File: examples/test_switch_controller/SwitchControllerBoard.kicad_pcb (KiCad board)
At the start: 2 copper layers, 64 x 35 mm, 40 parts, among them J1 COM-15111 (Sparkfun), J2 PinHeader2.54 1x4 (Generic), J3 PinHeader2.54 1x4 (Generic), Q1 2N7002 (Changjiang Electronic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, Q2 AO3401A (Alpha & Omega Semico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, SW1 5.1mm switch, SW2 5.1mm switch, U1 LD1117S33TR (STMicroelectroni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, U2 ESP32-WROOM-32 (Espressif Sys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, U3 LMV321 (Texas Instruments), U4 Duck, U5 IdDots4

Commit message: wip
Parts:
- added C10: , Capacitor_SMD:C_0805_2012Metric, F.Cu at (175.8, 40.2)
- added C11: , Capacitor_SMD:C_0603_1608Metric, F.Cu at (184.4, 37.0)
- added C12: , Capacitor_SMD:C_0805_2012Metric, F.Cu at (175.8, 37.2)
- added C13: , Capacitor_SMD:C_0603_1608Metric, F.Cu at (204.1, 26.2)
- added C14: , Capacitor_SMD:C_0603_1608Metric, F.Cu at (204.1, 28.7)
- added C15: , Capacitor_SMD:C_0603_1608Metric, F.Cu at (204.1, 23.7)
- added C6: , Capacitor_SMD:C_0603_1608Metric, F.Cu at (175.5, 43.0)
- added C7: , Capacitor_SMD:C_0603_1608Metric, F.Cu at (180.0, 40.0)
- added C8: , Capacitor_SMD:C_0805_2012Metric, F.Cu at (180.2, 37.2)
- added C9: , Capacitor_SMD:C_0603_1608Metric, F.Cu at (179.6, 43.0)
- added J3: AFC01-S015FCA-00 (Jushuo), Connector_FFC-FPC:Hirose_FH12-15S-0.5SH_1x15-1MP_P0.50mm_Horizontal, F.Cu at (180.9, 26.0)
- added R7: , Resistor_SMD:R_0603_1608Metric, F.Cu at (184.0, 40.0)
- added U3: CP2102 (Silicon Labs), Package_DFN_QFN:QFN-28-1EP_5x5mm_P0.5mm_EP3.35x3.35mm, F.Cu at (198.5, 26.1)
- added U4: PESD5V0X1BT (Nexperia), Package_TO_SOT_SMD:SOT-23, F.Cu at (194.2, 38.0)
- renumbered C6 to C16, J3 to J4, R9 to R10, R10 to R11, R11 to R12, R12 to R13, R7 to R8, R8 to R9, U3 to U5, U4 to U6, U5 to U7
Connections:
- U2 pad 10: sw1.out -> lcd.spi.miso
- U2 pad 11: ledr.signal -> usb_uart.uart.rx
- U2 pad 12: ledg.signal -> usb_uart.uart.tx
- U2 pad 13: ledb.signal -> conn.uart.rx
- U2 pad 14: sw.control -> conn.uart.tx
- U2 pad 16: (no net) -> sw1.out
- U2 pad 23: (no net) -> ledr.signal
- U2 pad 26: (no net) -> ledg.signal
- U2 pad 27: (no net) -> ledb.signal
- U2 pad 28: (no net) -> lcd.cs
- U2 pad 29: (no net) -> lcd.reset
- U2 pad 30: (no net) -> lcd.dc
- U2 pad 37: (no net) -> sw.control
- U2 pad 8: conn.uart.rx -> lcd.spi.sck
- U2 pad 9: conn.uart.tx -> lcd.spi.mosi

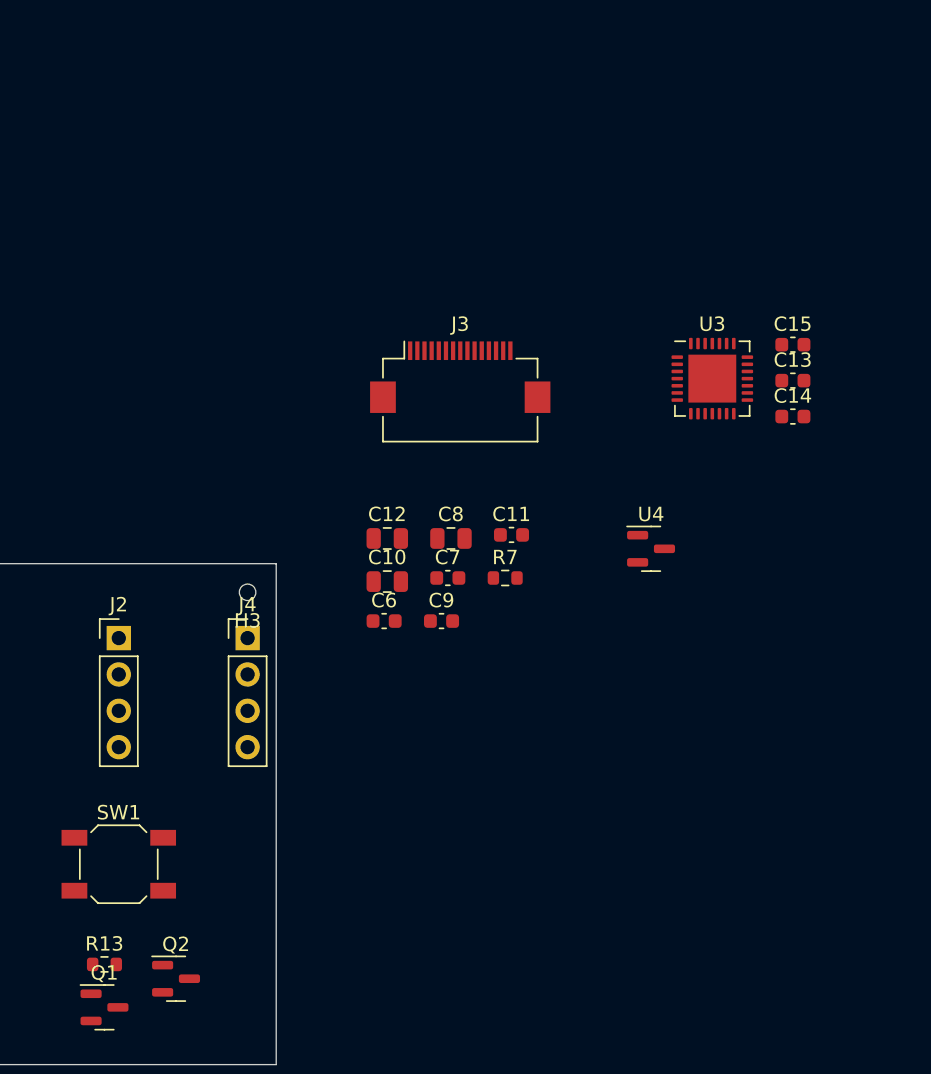
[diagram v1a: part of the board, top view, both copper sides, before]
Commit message: OLED outline
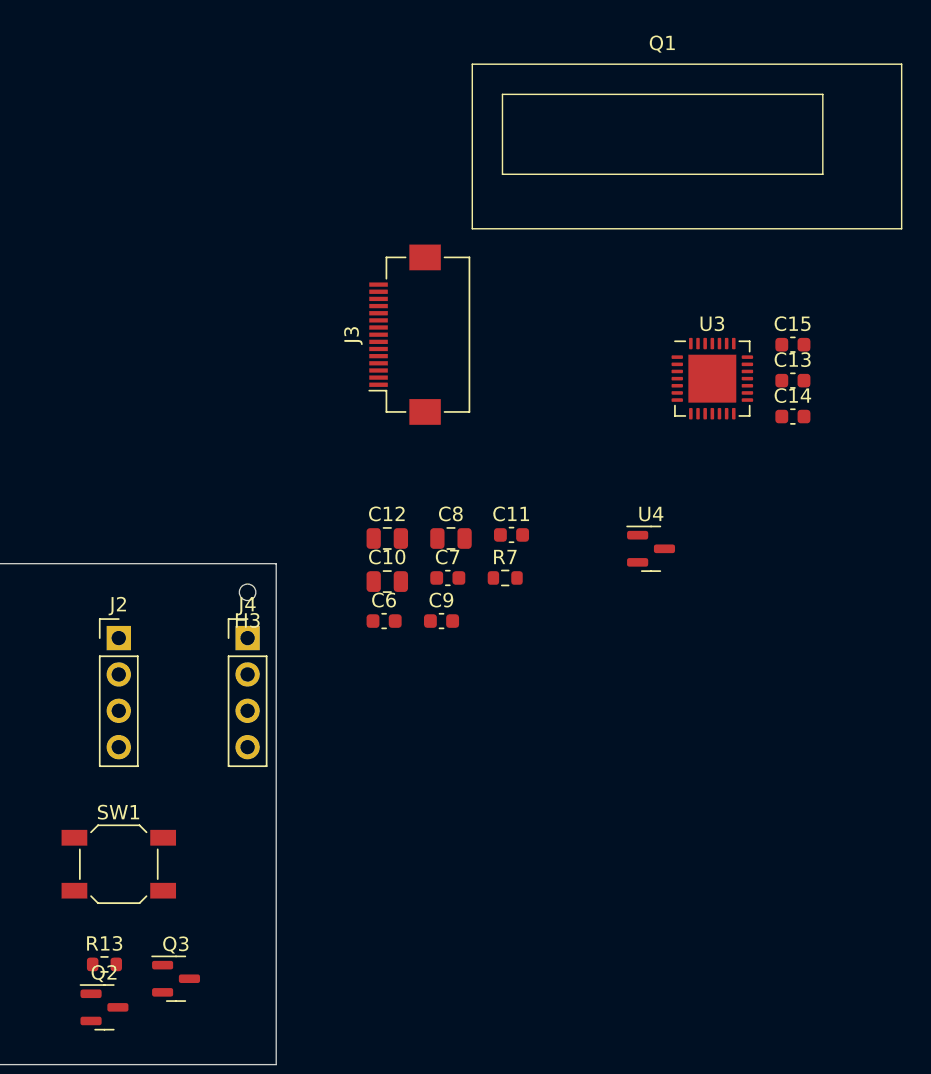
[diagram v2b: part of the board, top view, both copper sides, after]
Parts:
- added Q1: ER-OLED-0.91-e (EastRising), edg:Lcd_Er_Oled0.91_3_Outline, F.Cu at (195.0, 9.00)
- moved J3 4.87 mm to (177.0, 23.0), turned to 90 degrees
- renumbered Q1 to Q2, Q2 to Q3
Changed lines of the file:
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@@
   )
   (footprint "Connector_FFC-FPC:Hirose_FH12-15S-0.5SH_1x15-1MP_P0.50mm_Horizontal" (layer "F.Cu")
-    (at 180.86 25.97)
+    (at 177 23 90)
     (descr "Hirose FH12, FFC/FPC connector, FH12-15S-0.5SH, 15 Pins per row (https://www.hirose.com/product/en/products/FH12/FH12-24S-0.5SH(55)/), generated with kicad-footprint-generator")
     (tags "connector Hirose FH12 horizontal")
@@
     (property "edg_short_path" "lcd.device.conn")
     (attr smd)
-    (fp_text reference "J3" (at 0 -3.7) (layer "F.SilkS")
-      (effects (font (size 1 1) (thickness 0.15)))
-    )
-    (fp_text value "AFC01-S015FCA-00 (Jushuo)" (at 0 5.6) (layer "F.Fab")
-      (effects (font (size 1 1) (thickness 0.15)))
-    )
-    (fp_text user "${REFERENCE}" (at 0 3.7) (layer "F.Fab")
+    (fp_text reference "J3" (at 0 -3.7 90) (layer "F.SilkS")
+      (effects (font (size 1 1) (thickness 0.15)))
+    )
+    (fp_text value "AFC01-S015FCA-00 (Jushuo)" (at 0 5.6 90) (layer "F.Fab")
+      (effects (font (size 1 1) (thickness 0.15)))
+    )
+    (fp_text user "${REFERENCE}" (at 0 3.7 90) (layer "F.Fab")
       (effects (font (size 1 1) (thickness 0.15)))
     )
@@
     (fp_line (start 5.2 4.4) (end 0 4.4) (layer "F.Fab") (width 0.1))
     (fp_line (start -4.7 3.4) (end -4.7 3.7) (layer "F.Fab") (width 0.1))
-    (pad "1" smd rect (at -3.5 -1.85) (size 0.3 1.3) (layers "F.Cu" "F.Paste" "F.Mask")
+    (pad "1" smd rect (at -3.5 -1.85 90) (size 0.3 1.3) (layers "F.Cu" "F.Paste" "F.Mask")
       (net 47 "lcd.c2_cap.pos"))
-    (pad "2" smd rect (at -3 -1.85) (size 0.3 1.3) (layers "F.Cu" "F.Paste" "F.Mask")
+    (pad "2" smd rect (at -3 -1.85 90) (size 0.3 1.3) (layers "F.Cu" "F.Paste" "F.Mask")
       (net 48 "lcd.c2_cap.neg"))
-    (pad "3" smd rect (at -2.5 -1.85) (size 0.3 1.3) (layers "F.Cu" "F.Paste" "F.Mask")
+    (pad "3" smd rect (at -2.5 -1.85 90) (size 0.3 1.3) (layers "F.Cu" "F.Paste" "F.Mask")
       (net 49 "lcd.c1_cap.pos"))
-    (pad "4" smd rect (at -2 -1.85) (size 0.3 1.3) (layers "F.Cu" "F.Paste" "F.Mask")
+    (pad "4" smd rect (at -2 -1.85 90) (size 0.3 1.3) (layers "F.Cu" "F.Paste" "F.Mask")
       (net 50 "lcd.c1_cap.neg"))
-    (pad "5" smd rect (at -1.5 -1.85) (size 0.3 1.3) (layers "F.Cu" "F.Paste" "F.Mask")
+    (pad "5" smd rect (at -1.5 -1.85 90) (size 0.3 1.3) (layers "F.Cu" "F.Paste" "F.Mask")
       (net 17 "v3v3"))
-    (pad "6" smd rect (at -1 -1.85) (size 0.3 1.3) (layers "F.Cu" "F.Paste" "F.Mask")
-      (net 1 "gnd"))
-    (pad "7" smd rect (at -0.5 -1.85) (size 0.3 1.3) (layers "F.Cu" "F.Paste" "F.Mask")
+    (pad "6" smd rect (at -1 -1.85 90) (size 0.3 1.3) (layers "F.Cu" "F.Paste" "F.Mask")
+      (net 1 "gnd"))
+    (pad "7" smd rect (at -0.5 -1.85 90) (size 0.3 1.3) (layers "F.Cu" "F.Paste" "F.Mask")
       (net 17 "v3v3"))
-    (pad "8" smd rect (at 0 -1.85) (size 0.3 1.3) (layers "F.Cu" "F.Paste" "F.Mask")
+    (pad "8" smd rect (at 0 -1.85 90) (size 0.3 1.3) (layers "F.Cu" "F.Paste" "F.Mask")
       (net 35 "lcd.cs"))
-    (pad "9" smd rect (at 0.5 -1.85) (size 0.3 1.3) (layers "F.Cu" "F.Paste" "F.Mask")
+    (pad "9" smd rect (at 0.5 -1.85 90) (size 0.3 1.3) (layers "F.Cu" "F.Paste" "F.Mask")
       (net 36 "lcd.reset"))
-    (pad "10" smd rect (at 1 -1.85) (size 0.3 1.3) (layers "F.Cu" "F.Paste" "F.Mask")
+    (pad "10" smd rect (at 1 -1.85 90) (size 0.3 1.3) (layers "F.Cu" "F.Paste" "F.Mask")
       (net 37 "lcd.dc"))
-    (pad "11" smd rect (at 1.5 -1.85) (size 0.3 1.3) (layers "F.Cu" "F.Paste" "F.Mask")
+    (pad "11" smd rect (at 1.5 -1.85 90) (size 0.3 1.3) (layers "F.Cu" "F.Paste" "F.Mask")
       (net 30 "lcd.spi.sck"))
-    (pad "12" smd rect (at 2 -1.85) (size 0.3 1.3) (layers "F.Cu" "F.Paste" "F.Mask")
+    (pad "12" smd rect (at 2 -1.85 90) (size 0.3 1.3) (layers "F.Cu" "F.Paste" "F.Mask")
       (net 31 "lcd.spi.mosi"))
-    (pad "13" smd rect (at 2.5 -1.85) (size 0.3 1.3) (layers "F.Cu" "F.Paste" "F.Mask")
+    (pad "13" smd rect (at 2.5 -1.85 90) (size 0.3 1.3) (layers "F.Cu" "F.Paste" "F.Mask")
       (net 29 "lcd.iref_res.a"))
-    (pad "14" smd rect (at 3 -1.85) (size 0.3 1.3) (layers "F.Cu" "F.Paste" "F.Mask")
+    (pad "14" smd rect (at 3 -1.85 90) (size 0.3 1.3) (layers "F.Cu" "F.Paste" "F.Mask")
       (net 51 "lcd.device.vcomh"))
-    (pad "15" smd rect (at 3.5 -1.85) (size 0.3 1.3) (layers "F.Cu" "F.Paste" "F.Mask")
+    (pad "15" smd rect (at 3.5 -1.85 90) (size 0.3 1.3) (layers "F.Cu" "F.Paste" "F.Mask")
       (net 52 "lcd.device.vcc"))
-    (pad "MP" smd rect (at 5.4 1.4) (size 1.8 2.2) (layers "F.Cu" "F.Paste" "F.Mask"))
-    (pad "MP" smd rect (at -5.4 1.4) (size 1.8 2.2) (layers "F.Cu" "F.Paste" "F.Mask"))
+    (pad "MP" smd rect (at 5.4 1.4 90) (size 1.8 2.2) (layers "F.Cu" "F.Paste" "F.Mask"))
+    (pad "MP" smd rect (at -5.4 1.4 90) (size 1.8 2.2) (layers "F.Cu" "F.Paste" "F.Mask"))
     (model "${KICAD6_3DMODEL_DIR}/Connector_FFC-FPC.3dshapes/Hirose_FH12-15S-0.5SH_1x15-1MP_P0.50mm_Horizontal.wrl"
       (offset (xyz 0 0 0))
@@
     (property "edg_part" "2N7002 (Changjiang Electronics Tech (CJ))")
     (property "edg_path" "sw.pre")
-    (property "edg_refdes" "Q1")
+    (property "edg_refdes" "Q2")
     (property "edg_short_path" "sw.pre")
     (attr smd)
-    (fp_text reference "Q1" (at 0 -2.4) (layer "F.SilkS")
+    (fp_text reference "Q2" (at 0 -2.4) (layer "F.SilkS")
       (effects (font (size 1 1) (thickness 0.15)))
     )
@@
     (property "edg_part" "AO3401A (Alpha & Omega Semicon)")
     (property "edg_path" "sw.drv")
-    (property "edg_refdes" "Q2")
+    (property "edg_refdes" "Q3")
     (property "edg_short_path" "sw.drv")
     (attr smd)
-    (fp_text reference "Q2" (at 0 -2.4) (layer "F.SilkS")
+    (fp_text reference "Q3" (at 0 -2.4) (layer "F.SilkS")
       (effects (font (size 1 1) (thickness 0.15)))
     )
@@
     )
   )
+  (footprint "edg:Lcd_Er_Oled0.91_3_Outline" (layer "F.Cu")
+    (at 195 9)
+    (descr "Outline for the ER-OLED0.91-3 series OLEDs. Connector placement (on User.Comments layer, with FPC folded over underneath the board, for a bottom-entry FPC connector) is from the Reference Mechanical Design.")
+    (property "Sheetfile" "electronics_lib.Oled_Er_Oled_091_3.Er_Oled_091_3_Device")
+    (property "Sheetname" "device")
+    (property "edg_part" "ER-OLED-0.91-e (EastRising)")
+    (property "edg_path" "lcd.device.lcd")
+    (property "edg_refdes" "Q1")
+    (property "edg_short_path" "lcd.device.lcd")
+    (attr exclude_from_pos_files)
+    (fp_text reference "Q1" (at 0 -6.35) (layer "F.SilkS")
+      (effects (font (size 1 1) (thickness 0.15)))
+    )
+    (fp_text value "ER-OLED-0.91-e (EastRising)" (at 0 7.62) (layer "F.Fab")
+      (effects (font (size 1 1) (thickness 0.15)))
+    )
+    (fp_line (start -13.3 -4.9) (end -13.3 6.6) (layer "F.SilkS") (width 0.1))
+    (fp_line (start -11.192 -2.792) (end 11.192 -2.792) (layer "F.SilkS") (width 0.1))
+    (fp_line (start -13.3 6.6) (end 16.7 6.6) (layer "F.SilkS") (width 0.1))
+    (fp_line (start 16.7 -4.9) (end -13.3 -4.9) (layer "F.SilkS") (width 0.1))
+    (fp_line (start 11.192 -2.792) (end 11.192 2.792) (layer "F.SilkS") (width 0.1))
+    (fp_line (start 11.192 2.792) (end -11.192 2.792) (layer "F.SilkS") (width 0.1))
+    (fp_line (start -11.192 2.792) (end -11.192 -2.792) (layer "F.SilkS") (width 0.1))
+    (fp_line (start 16.7 6.6) (end 16.7 -4.9) (layer "F.SilkS") (width 0.1))
+    (fp_line (start 10.71 -2.04) (end 8.21 -2.04) (layer "Cmts.User") (width 0.12))
+    (fp_line (start 8.21 5.96) (end 10.71 5.96) (layer "Cmts.User") (width 0.12))
+    (fp_line (start 8.71 4.96) (end 8.71 4.96) (layer "Cmts.User") (width 0.25))
+    (fp_line (start 18.3 5.96) (end 18.3 -2.04) (layer "Cmts.User") (width 0.12))
+    (fp_line (start 8.21 5.96) (end 8.21 -2.04) (layer "Cmts.User") (width 0.12))
+  )
   (gr_rect (start 104 39) (end 168 74) (layer "Edge.Cuts") (width 0.0381) (fill none))

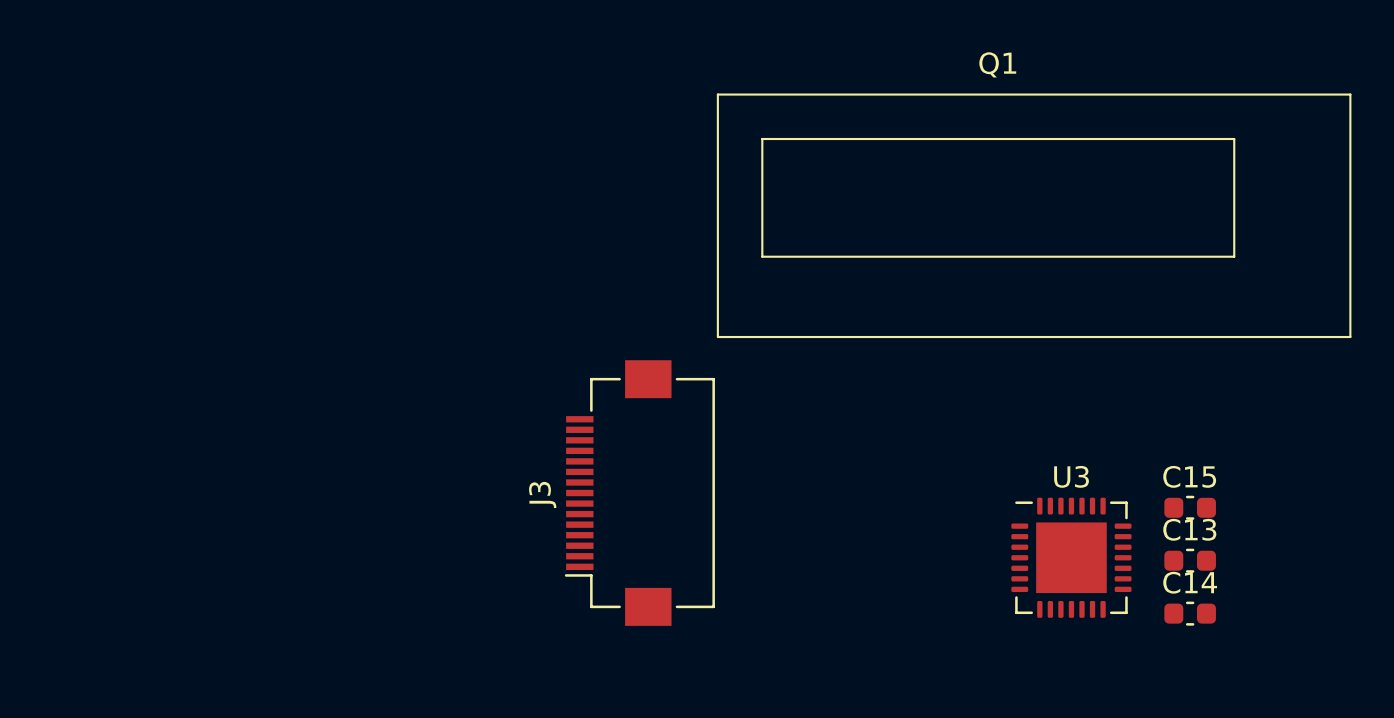
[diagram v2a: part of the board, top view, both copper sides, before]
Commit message: fix footprint
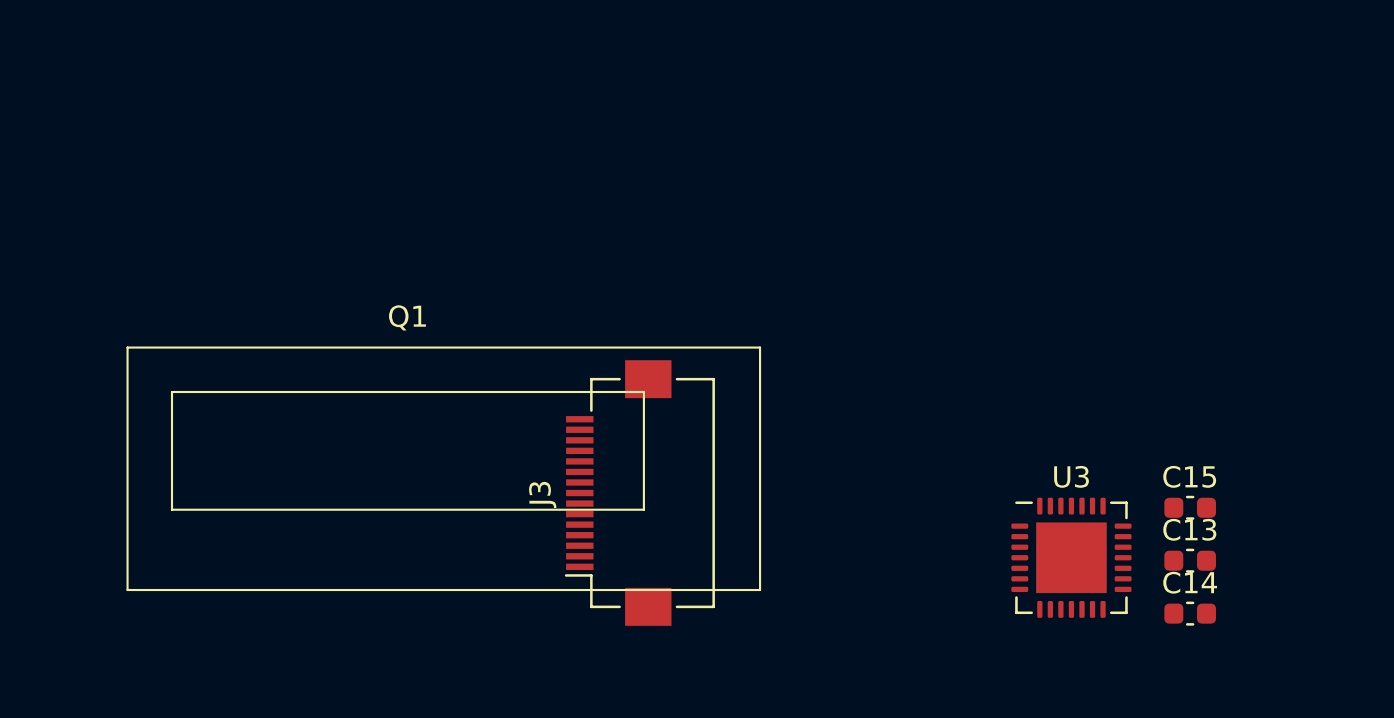
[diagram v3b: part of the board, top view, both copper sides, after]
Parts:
- moved Q1 30.5 mm to (167.0, 21.0)
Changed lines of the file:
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@@
     )
+  )
+  (footprint "edg:Lcd_Er_Oled0.91_3_Outline" (layer "F.Cu")
+    (at 167 21)
+    (descr "Outline for the ER-OLED0.91-3 series OLEDs. Connector placement (on User.Comments layer, with FPC folded over underneath the board, for a bottom-entry FPC connector) is from the Reference Mechanical Design.")
+    (property "Sheetfile" "electronics_lib.Oled_Er_Oled_091_3.Er_Oled_091_3_Device")
+    (property "Sheetname" "device")
+    (property "edg_part" "ER-OLED-0.91-e (EastRising)")
+    (property "edg_path" "lcd.device.lcd")
+    (property "edg_refdes" "Q1")
+    (property "edg_short_path" "lcd.device.lcd")
+    (attr exclude_from_pos_files)
+    (fp_text reference "Q1" (at 0 -6.35) (layer "F.SilkS")
+      (effects (font (size 1 1) (thickness 0.15)))
+    )
+    (fp_text value "ER-OLED-0.91-e (EastRising)" (at 0 7.62) (layer "F.Fab")
+      (effects (font (size 1 1) (thickness 0.15)))
+    )
+    (fp_line (start -13.3 6.6) (end 16.7 6.6) (layer "F.SilkS") (width 0.1))
+    (fp_line (start 11.192 2.792) (end -11.192 2.792) (layer "F.SilkS") (width 0.1))
+    (fp_line (start -13.3 -4.9) (end -13.3 6.6) (layer "F.SilkS") (width 0.1))
+    (fp_line (start 11.192 -2.792) (end 11.192 2.792) (layer "F.SilkS") (width 0.1))
+    (fp_line (start 16.7 6.6) (end 16.7 -4.9) (layer "F.SilkS") (width 0.1))
+    (fp_line (start -11.192 2.792) (end -11.192 -2.792) (layer "F.SilkS") (width 0.1))
+    (fp_line (start -11.192 -2.792) (end 11.192 -2.792) (layer "F.SilkS") (width 0.1))
+    (fp_line (start 16.7 -4.9) (end -13.3 -4.9) (layer "F.SilkS") (width 0.1))
+    (fp_line (start 10.71 -2.04) (end 8.21 -2.04) (layer "Cmts.User") (width 0.12))
+    (fp_line (start 8.21 5.96) (end 8.21 -2.04) (layer "Cmts.User") (width 0.12))
+    (fp_line (start 8.71 5.46) (end 8.71 5.46) (layer "Cmts.User") (width 0.25))
+    (fp_line (start 8.21 5.96) (end 10.71 5.96) (layer "Cmts.User") (width 0.12))
+    (fp_line (start 18.3 5.96) (end 18.3 -2.04) (layer "Cmts.User") (width 0.12))
   )
   (footprint "Package_TO_SOT_SMD:SOT-223-3_TabPin2" (layer "F.Cu")
@@
     )
   )
-  (footprint "edg:Lcd_Er_Oled0.91_3_Outline" (layer "F.Cu")
-    (at 195 9)
-    (descr "Outline for the ER-OLED0.91-3 series OLEDs. Connector placement (on User.Comments layer, with FPC folded over underneath the board, for a bottom-entry FPC connector) is from the Reference Mechanical Design.")
-    (property "Sheetfile" "electronics_lib.Oled_Er_Oled_091_3.Er_Oled_091_3_Device")
-    (property "Sheetname" "device")
-    (property "edg_part" "ER-OLED-0.91-e (EastRising)")
-    (property "edg_path" "lcd.device.lcd")
-    (property "edg_refdes" "Q1")
-    (property "edg_short_path" "lcd.device.lcd")
-    (attr exclude_from_pos_files)
-    (fp_text reference "Q1" (at 0 -6.35) (layer "F.SilkS")
-      (effects (font (size 1 1) (thickness 0.15)))
-    )
-    (fp_text value "ER-OLED-0.91-e (EastRising)" (at 0 7.62) (layer "F.Fab")
-      (effects (font (size 1 1) (thickness 0.15)))
-    )
-    (fp_line (start -13.3 -4.9) (end -13.3 6.6) (layer "F.SilkS") (width 0.1))
-    (fp_line (start -11.192 -2.792) (end 11.192 -2.792) (layer "F.SilkS") (width 0.1))
-    (fp_line (start -13.3 6.6) (end 16.7 6.6) (layer "F.SilkS") (width 0.1))
-    (fp_line (start 16.7 -4.9) (end -13.3 -4.9) (layer "F.SilkS") (width 0.1))
-    (fp_line (start 11.192 -2.792) (end 11.192 2.792) (layer "F.SilkS") (width 0.1))
-    (fp_line (start 11.192 2.792) (end -11.192 2.792) (layer "F.SilkS") (width 0.1))
-    (fp_line (start -11.192 2.792) (end -11.192 -2.792) (layer "F.SilkS") (width 0.1))
-    (fp_line (start 16.7 6.6) (end 16.7 -4.9) (layer "F.SilkS") (width 0.1))
-    (fp_line (start 10.71 -2.04) (end 8.21 -2.04) (layer "Cmts.User") (width 0.12))
-    (fp_line (start 8.21 5.96) (end 10.71 5.96) (layer "Cmts.User") (width 0.12))
-    (fp_line (start 8.71 4.96) (end 8.71 4.96) (layer "Cmts.User") (width 0.25))
-    (fp_line (start 18.3 5.96) (end 18.3 -2.04) (layer "Cmts.User") (width 0.12))
-    (fp_line (start 8.21 5.96) (end 8.21 -2.04) (layer "Cmts.User") (width 0.12))
-  )
   (gr_rect (start 104 39) (end 168 74) (layer "Edge.Cuts") (width 0.0381) (fill none))
